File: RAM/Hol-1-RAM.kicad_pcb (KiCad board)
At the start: 2 copper layers, 109.2 x 78.7 mm, 22 parts, among them P1 ADDRESS PORT, P2 DATA PORT, P3 DATA BUS, P4 Power, U1 74LS139, U10 74LS04, U11 74LS04, U12 74LS245, U2 74LS189, U3 74LS189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

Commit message: v1.0.4 rotated blinkenlight plugin to identify GND
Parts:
- turned JP1 to 90 degrees
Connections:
- JP1 pad 1: N-0000042 -> GND
- JP1 pad 2: N-0000043 -> N-0000038
- JP1 pad 3: N-0000044 -> N-0000037
- JP1 pad 4: N-0000041 -> N-0000034
- JP1 pad 6: N-0000033 -> N-0000041
- JP1 pad 7: N-0000037 -> N-0000042
- JP1 pad 8: N-0000038 -> N-0000043
- JP1 pad 9: GND -> N-0000044
- U11 pad 2: N-0000042 -> N-0000044
- U11 pad 4: N-0000044 -> N-0000042
- U11 pad 8: N-0000033 -> N-0000034
- U12 pad 2: N-0000042 -> N-0000044
- U12 pad 4: N-0000044 -> N-0000042
- U12 pad 7: N-0000033 -> N-0000034
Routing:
- net N-0000034: track 0.00 -> 35.6 mm
- net N-0000033: track 35.6 -> 0.00 mm
- net GND: track 333.0 -> 328.9 mm
- net N-0000038: track 65.4 -> 62.9 mm
- net N-0000044: track 45.0 -> 42.4 mm
- net N-0000042: track 42.4 -> 45.0 mm

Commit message: v1.2.1 updated schematic and pcb pictures
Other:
- board text added: "Address Bus"
- board text added: "Memory Input"
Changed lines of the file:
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@@
     (area 104.064999 63.424999 213.435001 142.684501)
     (thickness 1.6)
-    (drawings 9)
+    (drawings 11)
     (tracks 655)
     (zones 0)
@@
   )
   (setup
-    (last_trace_width 0.508)
+    (last_trace_width 0.254)
     (user_trace_width 0.508)
     (trace_clearance 0.254)
@@
       (rotate (xyz 0 0 0))
     )
+  )
+  (gr_text "Memory Input" (at 105.41 80.01 270) (layer F.SilkS)
+    (effects (font (size 1.5 1.5) (thickness 0.3)))
+  )
+  (gr_text "Address Bus" (at 105.41 124.46 270) (layer F.SilkS)
+    (effects (font (size 1.5 1.5) (thickness 0.3)))
   )
   (gr_line (start 104.14 139.7) (end 104.14 142.24) (angle 90) (layer Edge.Cuts) (width 0.15))
@@
   (segment (start 178.435 99.06) (end 180.34 99.06) (width 0.254) (layer B.Cu) (net 27))
   (segment (start 178.435 71.12) (end 178.435 99.06) (width 0.254) (layer B.Cu) (net 27))
-  (segment (start 193.04 139.7) (end 193.04 141.605) (width 0.508) (layer B.Cu) (net 28) (status 400000))
+  (segment (start 193.04 139.7) (end 193.04 141.605) (width 0.508) (layer B.Cu) (net 28))
   (segment (start 193.04 141.605) (end 182.88 141.606116) (width 0.508) (layer B.Cu) (net 28))
-  (segment (start 193.04 139.7) (end 198.12 139.7) (width 0.508) (layer B.Cu) (net 28) (status C00000))
+  (segment (start 193.04 139.7) (end 198.12 139.7) (width 0.508) (layer B.Cu) (net 28))
   (segment (start 193.04 139.7) (end 193.04 139.7) (width 0.254) (layer B.Cu) (net 28))
   (segment (start 162.56 139.7) (end 165.103393 139.7) (width 0.508) (layer B.Cu) (net 28))
@@
   (segment (start 148.59 137.16) (end 148.59 140.97) (width 0.254) (layer F.Cu) (net 32))
   (segment (start 148.59 140.335) (end 148.59 140.97) (width 0.254) (layer F.Cu) (net 32))
-  (segment (start 193.04 127) (end 185.42 127) (width 0.254) (layer F.Cu) (net 33) (status 400000))
+  (segment (start 193.04 127) (end 185.42 127) (width 0.254) (layer F.Cu) (net 33))
   (segment (start 185.42 134.62) (end 185.42 127) (width 0.254) (layer F.Cu) (net 33))
   (segment (start 185.42 134.62) (end 170.18 134.62) (width 0.254) (layer F.Cu) (net 33))
-  (segment (start 193.04 127) (end 198.12 127) (width 0.254) (layer F.Cu) (net 33) (status C00000))
+  (segment (start 193.04 127) (end 198.12 127) (width 0.254) (layer F.Cu) (net 33))
   (segment (start 193.04 124.46) (end 184.15 124.46) (width 0.254) (layer F.Cu) (net 34))
   (segment (start 163.83 133.35) (end 184.15 133.35) (width 0.254) (layer F.Cu) (net 34))

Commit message: v1.3.6 silkscreen IC footprint corrections
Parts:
- U1, U2, U3, U4, U5, U6, U7, U8, U9: footprint DIP-16__300 -> DIP-16
- U10, U11: footprint DIP-14__300 -> DIP-14
- U12: footprint DIP-20__300 -> DIP-20
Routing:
- net N-0000049: track 83.8 -> 76.4 mm
- net N-0000048: track 77.5 -> 70.8 mm
- net N-0000047: track 71.1 -> 65.2 mm
- net N-0000046: track 64.8 -> 59.6 mm
- net N-0000050: track 58.4 -> 54.0 mm
- net N-0000055: track 52.1 -> 48.4 mm
- net N-0000054: track 45.7 -> 42.7 mm
- net N-0000053: track 39.4 -> 37.1 mm
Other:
- board text added: "+5v Gnd"
- board text added: "DATA BUS"

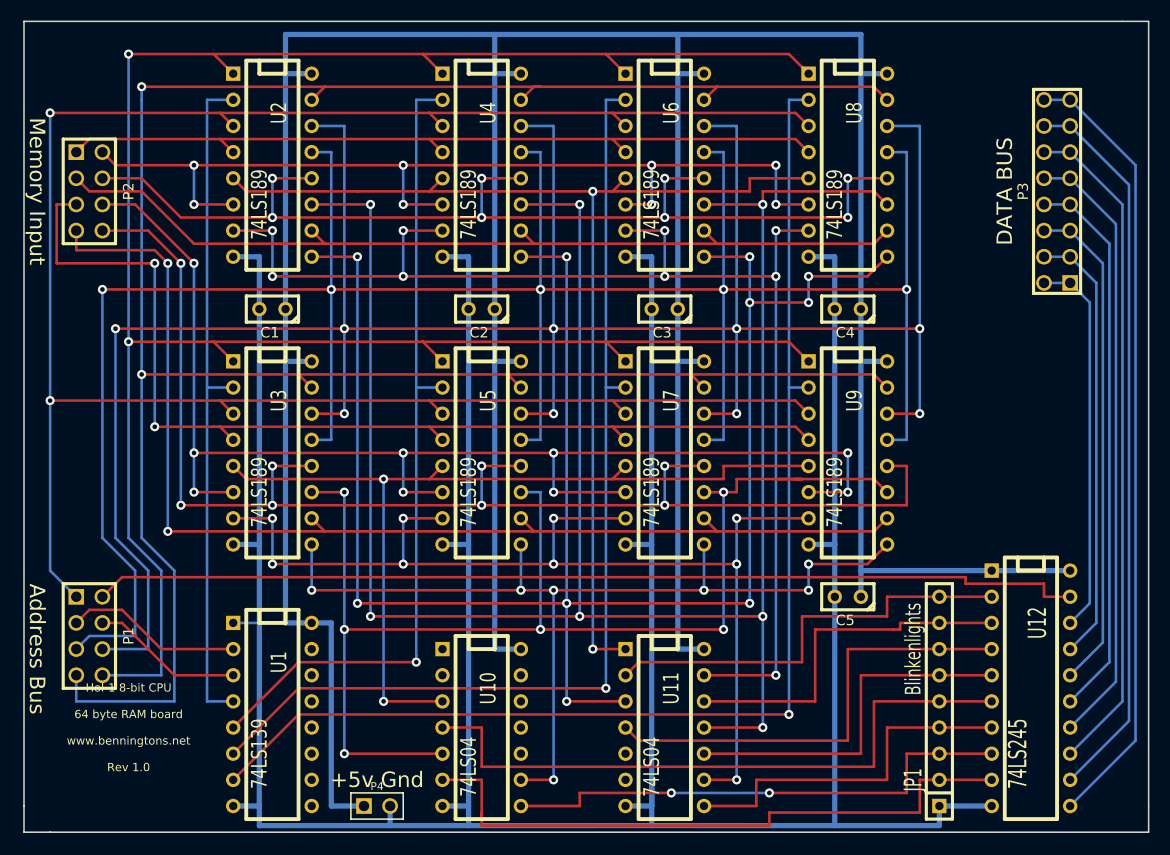
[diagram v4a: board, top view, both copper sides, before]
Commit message: 1.5.21 upgraded to KiCad 6.0
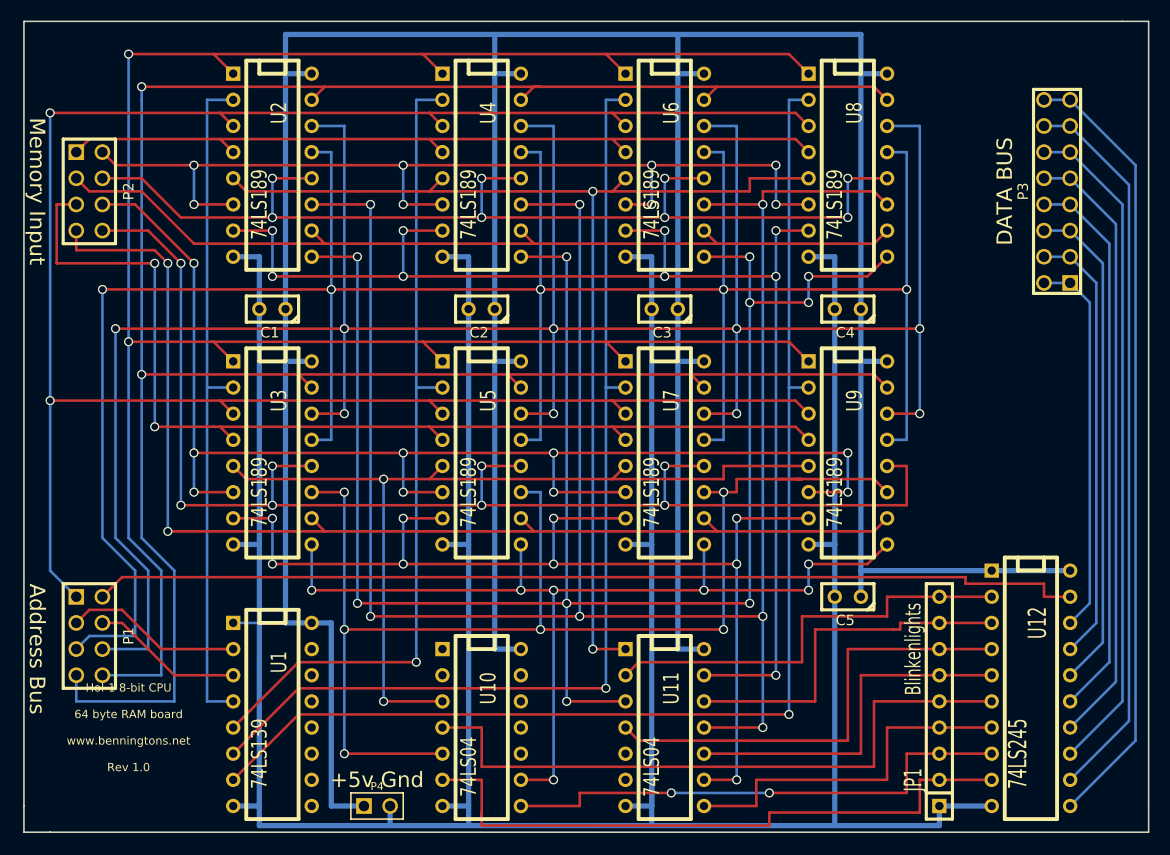
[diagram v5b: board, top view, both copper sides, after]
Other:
- net class Default removed
